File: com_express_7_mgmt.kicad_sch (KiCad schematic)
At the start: 1 part, among them J1 Plug_Bus_CE7_EPT_401-55501-51

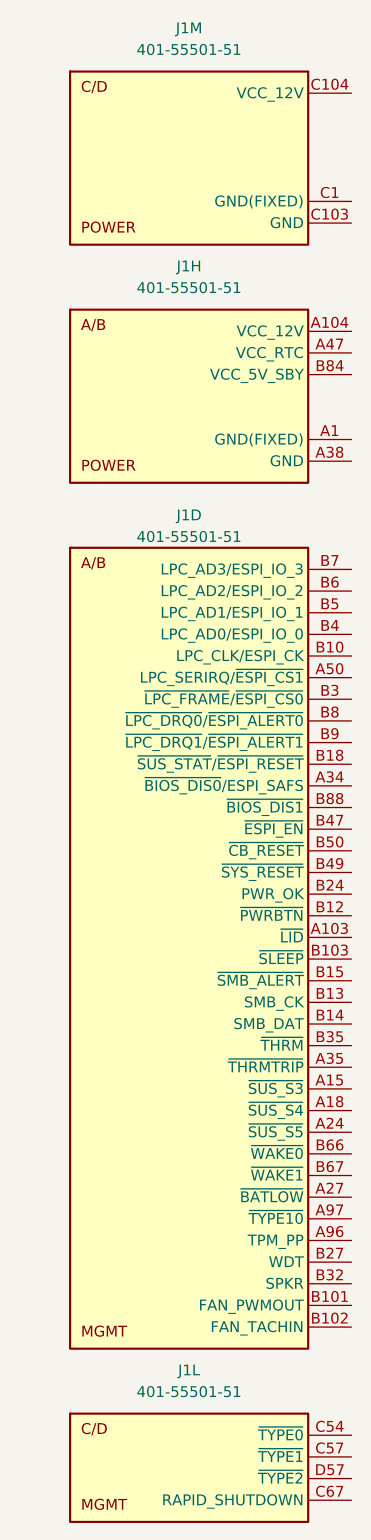
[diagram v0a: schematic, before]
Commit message: [#57056] Create schematics for M.2 and OCuLink connectors
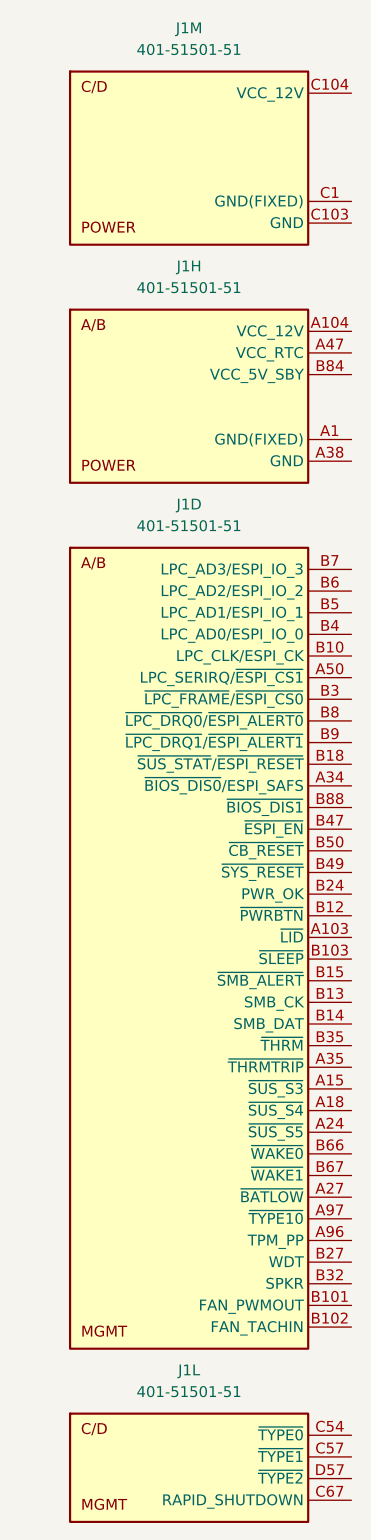
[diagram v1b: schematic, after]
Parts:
- J1: value Plug_Bus_CE7_EPT_401-55501-51 -> Plug_Bus_CE7_EPT_401-51501-51; footprint antmicro-footprints:EPT_401-55501-51 -> antmicro-footprints:EPT_401-51501-51; symbol antmicroB2BConnectors:Plug_Bus_CE7_EPT_401-55501-51 -> antmicroB2BConnectors:Plug_Bus_CE7_EPT_401-51501-51; MPN 401-55501-51 -> 401-51501-51
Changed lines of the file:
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@@
     (company "Antmicro Ltd.")
   )
-  (symbol (lib_id "antmicroB2BConnectors:Plug_Bus_CE7_EPT_401-55501-51") (at 60.96 38.1 0) (unit 13)
+  (symbol (lib_id "antmicroB2BConnectors:Plug_Bus_CE7_EPT_401-51501-51") (at 60.96 38.1 0) (unit 13)
     (in_bom yes) (on_board yes) (dnp no) (fields_autoplaced)
     (property "Reference" "J1" (at 41.91 30.48 0)
       (effects (font (size 1.27 1.27) (thickness 0.15)))
     )
-    (property "Value" "Plug_Bus_CE7_EPT_401-55501-51" (at 114.3 50.8 0)
-      (effects (font (size 1.27 1.27) (thickness 0.15)) (justify left bottom) hide)
-    )
-    (property "Footprint" "antmicro-footprints:EPT_401-55501-51" (at 114.3 53.34 0)
+    (property "Value" "Plug_Bus_CE7_EPT_401-51501-51" (at 114.3 50.8 0)
+      (effects (font (size 1.27 1.27) (thickness 0.15)) (justify left bottom) hide)
+    )
+    (property "Footprint" "antmicro-footprints:EPT_401-51501-51" (at 114.3 53.34 0)
       (effects (font (size 1.27 1.27) (thickness 0.15)) (justify left bottom) hide)
     )
@@
       (effects (font (size 1.27 1.27) (thickness 0.15)) (justify left bottom) hide)
     )
-    (property "MPN" "401-55501-51" (at 41.91 33.02 0)
+    (property "MPN" "401-51501-51" (at 41.91 33.02 0)
       (effects (font (size 1.27 1.27) (thickness 0.15)))
     )
@@
     )
   )
-  (symbol (lib_id "antmicroB2BConnectors:Plug_Bus_CE7_EPT_401-55501-51") (at 60.96 66.04 0) (unit 8)
+  (symbol (lib_id "antmicroB2BConnectors:Plug_Bus_CE7_EPT_401-51501-51") (at 60.96 66.04 0) (unit 8)
     (in_bom yes) (on_board yes) (dnp no) (fields_autoplaced)
     (property "Reference" "J1" (at 41.91 58.42 0)
       (effects (font (size 1.27 1.27) (thickness 0.15)))
     )
-    (property "Value" "Plug_Bus_CE7_EPT_401-55501-51" (at 114.3 78.74 0)
-      (effects (font (size 1.27 1.27) (thickness 0.15)) (justify left bottom) hide)
-    )
-    (property "Footprint" "antmicro-footprints:EPT_401-55501-51" (at 114.3 81.28 0)
+    (property "Value" "Plug_Bus_CE7_EPT_401-51501-51" (at 114.3 78.74 0)
+      (effects (font (size 1.27 1.27) (thickness 0.15)) (justify left bottom) hide)
+    )
+    (property "Footprint" "antmicro-footprints:EPT_401-51501-51" (at 114.3 81.28 0)
       (effects (font (size 1.27 1.27) (thickness 0.15)) (justify left bottom) hide)
     )
@@
       (effects (font (size 1.27 1.27) (thickness 0.15)) (justify left bottom) hide)
     )
-    (property "MPN" "401-55501-51" (at 41.91 60.96 0)
+    (property "MPN" "401-51501-51" (at 41.91 60.96 0)
       (effects (font (size 1.27 1.27) (thickness 0.15)))
     )
@@
     )
   )
-  (symbol (lib_id "antmicroB2BConnectors:Plug_Bus_CE7_EPT_401-55501-51") (at 60.96 195.58 0) (unit 12)
+  (symbol (lib_id "antmicroB2BConnectors:Plug_Bus_CE7_EPT_401-51501-51") (at 60.96 195.58 0) (unit 12)
     (in_bom yes) (on_board yes) (dnp no) (fields_autoplaced)
     (property "Reference" "J1" (at 41.91 187.96 0)
       (effects (font (size 1.27 1.27) (thickness 0.15)))
     )
-    (property "Value" "Plug_Bus_CE7_EPT_401-55501-51" (at 114.3 208.28 0)
-      (effects (font (size 1.27 1.27) (thickness 0.15)) (justify left bottom) hide)
-    )
-    (property "Footprint" "antmicro-footprints:EPT_401-55501-51" (at 114.3 210.82 0)
+    (property "Value" "Plug_Bus_CE7_EPT_401-51501-51" (at 114.3 208.28 0)
+      (effects (font (size 1.27 1.27) (thickness 0.15)) (justify left bottom) hide)
+    )
+    (property "Footprint" "antmicro-footprints:EPT_401-51501-51" (at 114.3 210.82 0)
       (effects (font (size 1.27 1.27) (thickness 0.15)) (justify left bottom) hide)
     )
@@
       (effects (font (size 1.27 1.27) (thickness 0.15)) (justify left bottom) hide)
     )
-    (property "MPN" "401-55501-51" (at 41.91 190.5 0)
+    (property "MPN" "401-51501-51" (at 41.91 190.5 0)
       (effects (font (size 1.27 1.27) (thickness 0.15)))
     )
@@
     )
   )
-  (symbol (lib_id "antmicroB2BConnectors:Plug_Bus_CE7_EPT_401-55501-51") (at 60.96 93.98 0) (unit 4)
+  (symbol (lib_id "antmicroB2BConnectors:Plug_Bus_CE7_EPT_401-51501-51") (at 60.96 93.98 0) (unit 4)
     (in_bom yes) (on_board yes) (dnp no) (fields_autoplaced)
-    (property "Reference" "J1" (at 41.91 87.63 0)
+    (property "Reference" "J1" (at 41.91 86.36 0)
       (effects (font (size 1.27 1.27) (thickness 0.15)))
     )
-    (property "Value" "Plug_Bus_CE7_EPT_401-55501-51" (at 114.3 106.68 0)
-      (effects (font (size 1.27 1.27) (thickness 0.15)) (justify left bottom) hide)
-    )
-    (property "Footprint" "antmicro-footprints:EPT_401-55501-51" (at 114.3 109.22 0)
+    (property "Value" "Plug_Bus_CE7_EPT_401-51501-51" (at 114.3 106.68 0)
+      (effects (font (size 1.27 1.27) (thickness 0.15)) (justify left bottom) hide)
+    )
+    (property "Footprint" "antmicro-footprints:EPT_401-51501-51" (at 114.3 109.22 0)
       (effects (font (size 1.27 1.27) (thickness 0.15)) (justify left bottom) hide)
     )
@@
       (effects (font (size 1.27 1.27) (thickness 0.15)) (justify left bottom) hide)
     )
-    (property "MPN" "401-55501-51" (at 41.91 90.17 0)
+    (property "MPN" "401-51501-51" (at 41.91 88.9 0)
       (effects (font (size 1.27 1.27) (thickness 0.15)))
     )

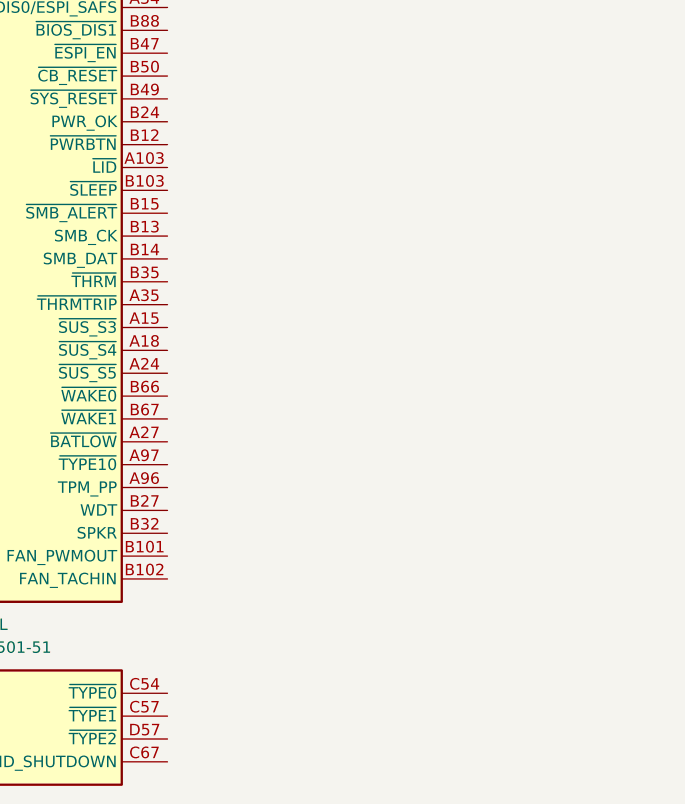
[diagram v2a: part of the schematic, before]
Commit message: [#57056] Add GPIO expander. Connect GPIOs and SMBus lines
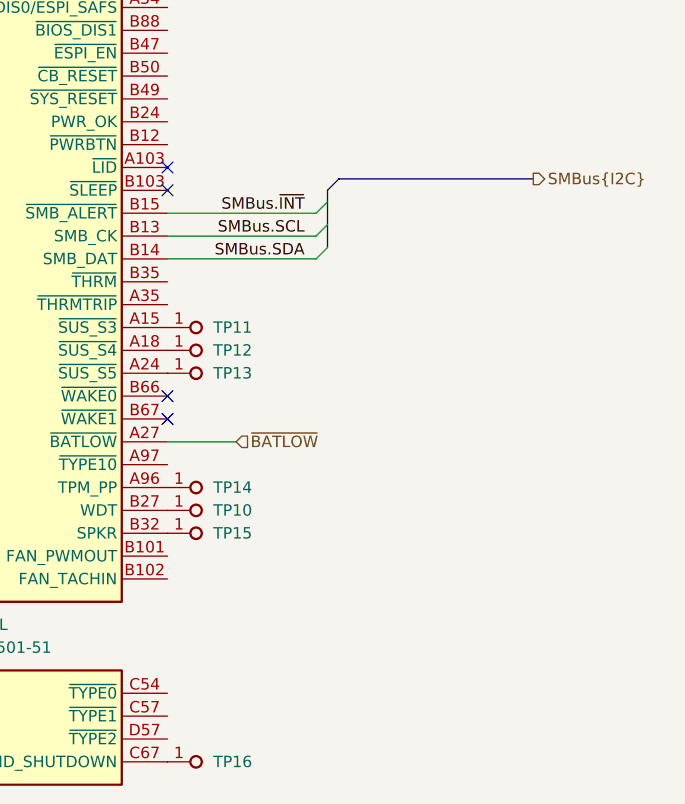
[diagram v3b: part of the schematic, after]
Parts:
- added TP10, TP11, TP12, TP13, TP14, TP15, TP16: TP_0.75mm_SMD, antmicro-footprints:TP_SMD_0.75mm, symbol antmicroTestPoints:TP_0.75mm_SMD
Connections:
- net at J1.C67 (RAPID_SHUTDOWN): now also TP16.1
- net at J1.A15 (~{SUS_S3}): now also TP11.1
- net at J1.A18 (~{SUS_S4}): now also TP12.1
- net at J1.A24 (~{SUS_S5}): now also TP13.1
- net ~{BATLOW}: now reaches J1.A27 (~{BATLOW})
- net at J1.A96 (TPM_PP): now also TP14.1
- net SMBus.SCL: now reaches J1.B13 (SMB_CK)
- net SMBus.SDA: now reaches J1.B14 (SMB_DAT)
- net SMBus.~{INT}: now reaches J1.B15 (~{SMB_ALERT})
- net at J1.B27 (WDT): now also TP10.1
- net at J1.B32 (SPKR): now also TP15.1
- no-connect marks 0 -> 4

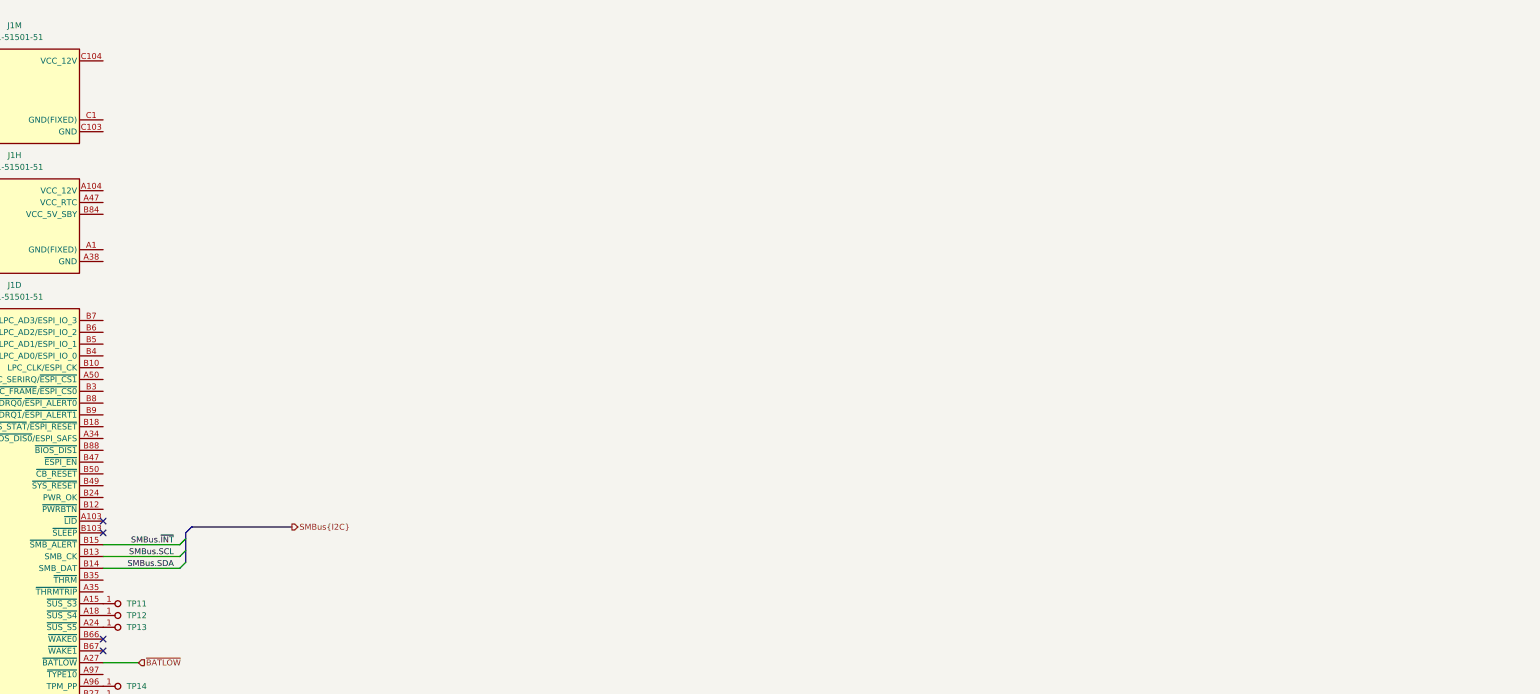
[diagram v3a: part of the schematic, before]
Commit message: [#57905] Add power and reset circuitry
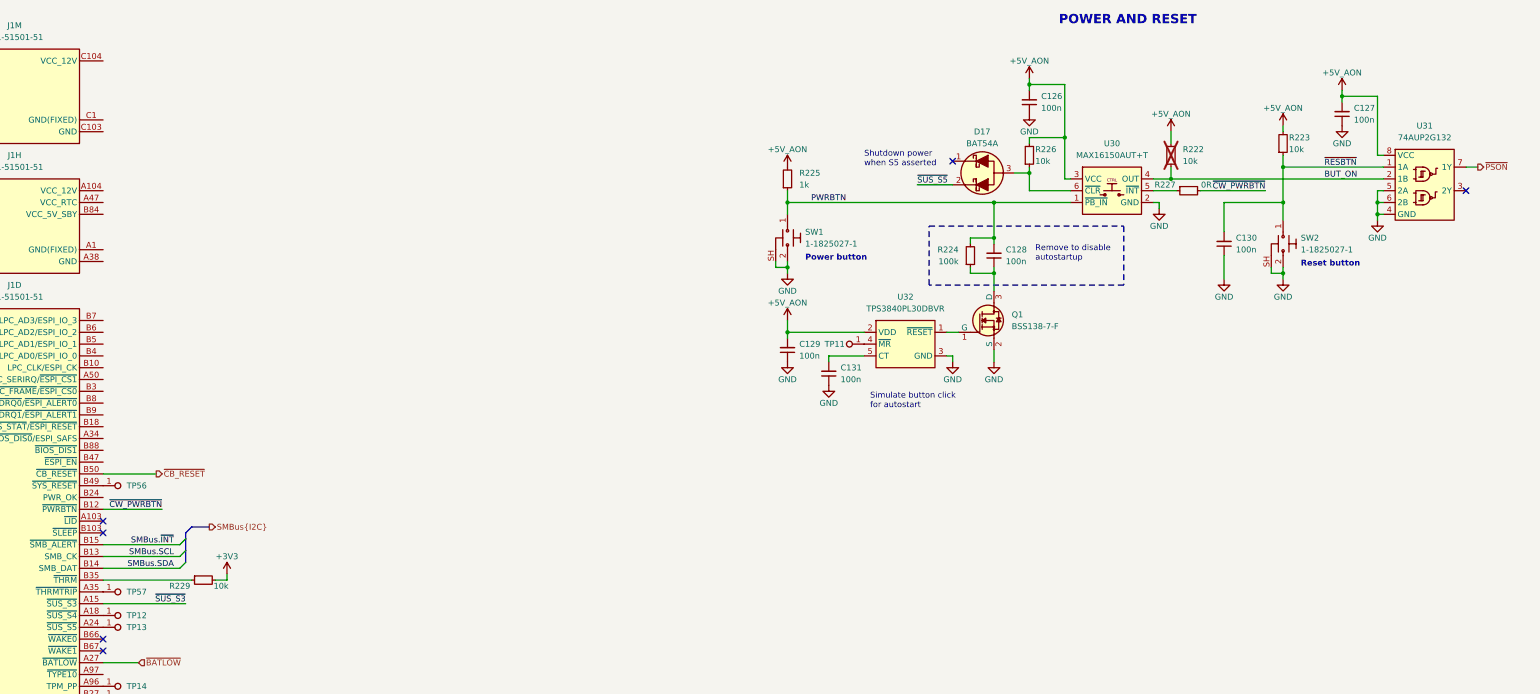
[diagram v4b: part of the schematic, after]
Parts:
- added C126, C127, C128, C129, C130, C131: C_100n_0402, antmicro-footprints:C_0402_1005Metric, symbol antmicroCapacitors0402:C_100n_0402
- added D17: BAT54A, antmicro-footprints:SOT-23-3, symbol antmicroDiodesRectifiersSingle:BAT54A
- added Q1: BSS138-7-F, antmicro-footprints:SOT-23-3, symbol antmicroTransistorsFETsMOSFETsSingle:BSS138-7-F
- added R222, R223, R226, R229: R_10k_0402, antmicro-footprints:R_0402_1005Metric, symbol antmicroResistors0402:R_10k_0402
- added R224: R_100k_0402, antmicro-footprints:R_0402_1005Metric, symbol antmicroResistors0402:R_100k_0402
- added R225: R_1k_0402, antmicro-footprints:R_0402_1005Metric, symbol antmicroResistors0402:R_1k_0402
- added R227: R_0R_0402, antmicro-footprints:R_0402_1005Metric, symbol antmicroResistors0402:R_0R_0402
- added SW1, SW2: SW_1-1825027-1_THT, antmicro-footprints:SW_1-1825027-1_THT, symbol antmicroPushbuttonSwitches:SW_1-1825027-1_THT
- added TP56, TP57: TP_0.75mm_SMD, antmicro-footprints:TP_SMD_0.75mm, symbol antmicroTestPoints:TP_0.75mm_SMD
- added U30: MAX16150A_SOT, antmicro-footprints:SOT-23-6, symbol antmicroPMICPowerSequencers:MAX16150A_SOT
- added U31: 74AUP2G132, antmicro-footprints:VSSOP-8_2.3x2mm_P0.5mm, symbol antmicroLogicGatesandInverters:74AUP2G132
- added U32: TPS3840PL30DBVR, antmicro-footprints:SOT-23-5, symbol antmicroPMICPowerSequencers:TPS3840PL30DBVR
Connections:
- net at TP11.1: now also U32.4 (~{MR}); no longer J1.A15 (~{SUS_S3})
- net at J1.A35 (~{THRMTRIP}): now also TP57.1
- net ~{CW_PWRBTN}: now reaches J1.B12 (~{PWRBTN})
- net ~{CW_PWRBTN}: now also R227.2
- net at J1.B35 (~{THRM}): now also R229.1
- net at J1.B49 (~{SYS_RESET}): now also TP56.1
- net ~{CB_RESET}: now reaches J1.B50 (~{CB_RESET})
- new net: C128.1, Q1.3 (D), R224.1
- new net: D17.3, R226.1, U30.6 (~{CLR})
- new net: C131.2, U32.5 (CT)
- new net: Q1.1 (G), U32.1 (~{RESET})
- new net: R227.1, U30.5 (~{INT})
- new net +3V3: R229.2
- new net +5V_AON: C126.2, C127.2, C129.2, R222.2, R223.2, R225.2, R226.2, U30.3 (VCC), U31.8 (VCC), U32.2 (VDD)
- new net BUT_ON: R222.1, U30.4 (OUT), U31.2 (1B)
- new net GND: C126.1, C127.1, C129.1, C130.1, C131.1, Q1.2 (S), SW1.2, SW1.SH, SW2.2, SW2.SH, U30.2 (GND), U31.4 (GND), U31.5 (2A), U31.6 (2B), U32.3 (GND)
- new net PWRBTN: C128.2, R224.2, R225.1, SW1.1, U30.1 (~{PB_IN})
- new net ~{PSON}: U31.7 (1Y)
- new net ~{RESBTN}: C130.2, R223.1, SW2.1, U31.1 (1A)
- new net ~{SUS_S3}: J1.A15 (~{SUS_S3})
- new net ~{SUS_S5}: D17.2
- no-connect marks 4 -> 6
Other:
- note added: "POWER AND RESET"
- note added: "Power button"
- note added: "Remove to disable autostartup"
- note added: "Reset button"
- note added: "Shutdown power when S5 asserted"
- note added: "Simulate button click for autostart"

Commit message: [#57905] Add Type 7 check
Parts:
- removed D17: BAT54A, antmicro-footprints:SOT-23-3, symbol antmicroDiodesRectifiersSingle:BAT54A
- added C132: C_100n_0402, antmicro-footprints:C_0402_1005Metric, symbol antmicroCapacitors0402:C_100n_0402
- added D17: BAT54C, antmicro-footprints:SOT-23-3, symbol antmicroDiodesRectifiersSingle:BAT54C
- added Q2: BSS138-7-F, antmicro-footprints:SOT-23-3, symbol antmicroTransistorsFETsMOSFETsSingle:BSS138-7-F
- added R228, R230, R231: R_10k_0402, antmicro-footprints:R_0402_1005Metric, symbol antmicroResistors0402:R_10k_0402
- added R232: R_100k_0402, antmicro-footprints:R_0402_1005Metric, symbol antmicroResistors0402:R_100k_0402
- added R233: R_0R_0402, antmicro-footprints:R_0402_1005Metric, symbol antmicroResistors0402:R_0R_0402
- added TP58, TP59: TP_0.75mm_SMD, antmicro-footprints:TP_SMD_0.75mm, symbol antmicroTestPoints:TP_0.75mm_SMD
- added U33: 74AUP2G132, antmicro-footprints:VSSOP-8_2.3x2mm_P0.5mm, symbol antmicroLogicGatesandInverters:74AUP2G132
- R226: DNP (none) -> DNP; now not fitted
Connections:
- net GND: now also C132.1, Q2.2 (S), R232.1, U33.4 (GND)
- net ~{RESBTN}: now also Q2.3 (D)
- net ~{SUS_S5}: now also R233.2
- net at R226.1, U30.6 (~{CLR}): now also R233.1
- net ~{TYPE0}: now reaches J1.C54 (~{TYPE0})
- net ~{TYPE0}: now also D17.1, R228.1
- net ~{TYPE1}: now reaches J1.C57 (~{TYPE1})
- net ~{TYPE1}: now also R230.1, U33.6 (2B)
- net ~{TYPE2}: now reaches J1.D57 (~{TYPE2})
- net ~{TYPE2}: now also D17.2, R231.1
- net at J1.A97 (~{TYPE10}): now also TP59.1
- net FAN_PWM: now reaches J1.B101 (FAN_PWMOUT)
- net FAM_TACH: now reaches J1.B102 (FAN_TACHIN)
- net +5V_AON renamed +3V3_AON
- net +3V3_AON: now also C132.2, R228.2, R230.2, R231.2, U33.8 (VCC)
- net ~{BATLOW}: no longer names the net of J1.A27 (~{BATLOW})
- net ~{BATLOW}: now also TP58.1
- new net: D17.3, R232.2, U33.1 (1A), U33.2 (1B)
- new net: U33.5 (2A), U33.7 (1Y)
- new net ~{COM7}: Q2.1 (G), U33.3 (2Y)
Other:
- note added: "Check if module is type 7: ~{TYPE0} GND ~{TYPE1} NC ~{TYPE2} GND"
- moved on the sheet: C126, C127, C128, C129, C130, C131, J1D, J1H, J1L, J1M, Q1, R222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
